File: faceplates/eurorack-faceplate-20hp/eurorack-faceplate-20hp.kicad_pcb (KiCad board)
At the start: 2 copper layers, 101.3 x 133.3 mm, 4 parts

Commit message: Moving mounting holes
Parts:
- moved REF** 2.42 mm to (5.08, 130.3)
- moved REF** 2.42 mm to (5.08, 3.00)
- moved REF** 2.36 mm to (96.2, 130.3)
- moved REF** 2.36 mm to (96.2, 3.00)
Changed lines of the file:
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@@
   (net 0 "")
   (footprint "MountingHole:MountingHole_3.2mm_M3" (layer "F.Cu")
-    (at 7.5 130.35)
+    (at 5.08 130.35)
     (descr "Mounting Hole 3.2mm, no annular, M3")
     (tags "mounting hole 3.2mm no annular m3")
@@
   )
   (footprint "MountingHole:MountingHole_3.2mm_M3" (layer "F.Cu")
-    (at 93.86 130.35)
+    (at 96.22 130.35)
     (descr "Mounting Hole 3.2mm, no annular, M3")
     (tags "mounting hole 3.2mm no annular m3")
@@
   )
   (footprint "MountingHole:MountingHole_3.2mm_M3" (layer "F.Cu")
-    (at 93.86 3)
+    (at 96.22 3)
     (descr "Mounting Hole 3.2mm, no annular, M3")
     (tags "mounting hole 3.2mm no annular m3")
@@
   )
   (footprint "MountingHole:MountingHole_3.2mm_M3" (layer "F.Cu")
-    (at 7.5 3)
+    (at 5.08 3)
     (descr "Mounting Hole 3.2mm, no annular, M3")
     (tags "mounting hole 3.2mm no annular m3")

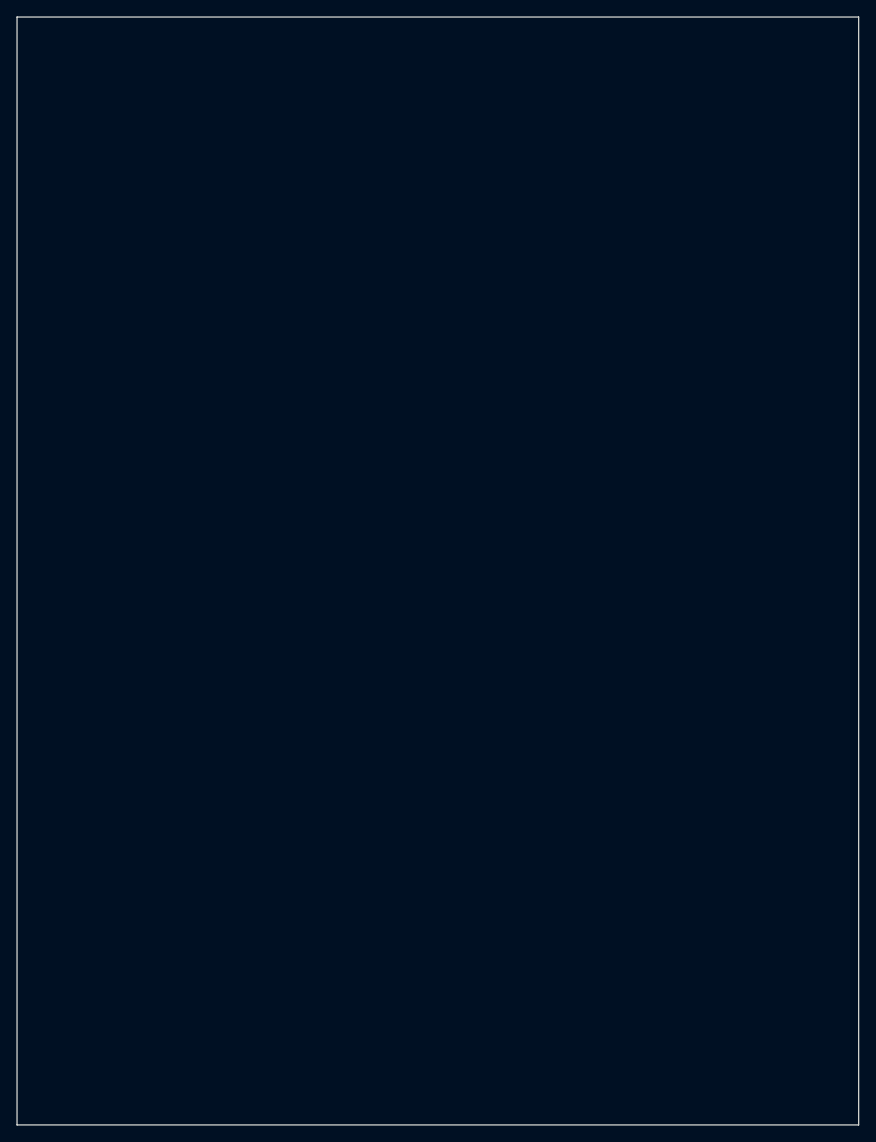
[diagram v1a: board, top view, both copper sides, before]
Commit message: Correcting panel height
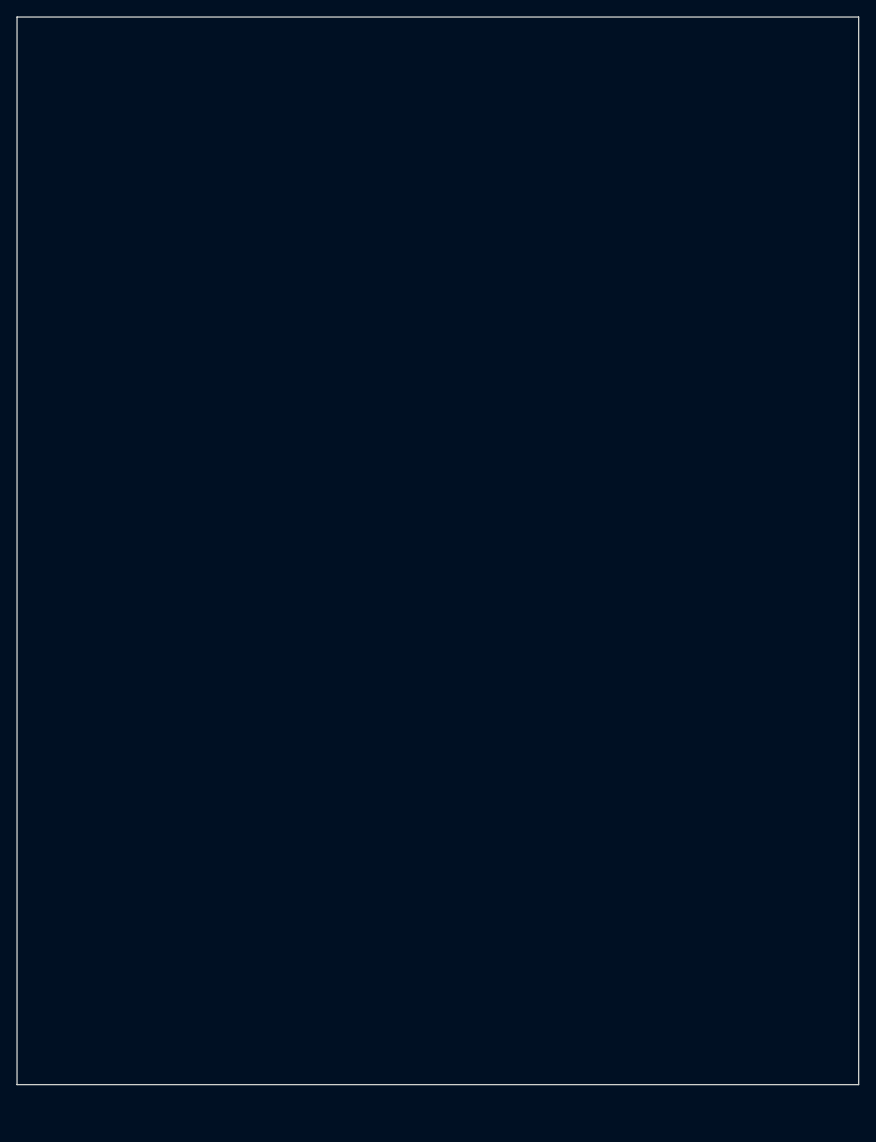
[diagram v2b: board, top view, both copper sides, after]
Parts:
- moved REF** 4.85 mm to (5.08, 125.5)
- moved REF** 4.85 mm to (96.2, 125.5)
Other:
- board size 101.3 x 133.3 mm -> 101.3 x 128.5 mm
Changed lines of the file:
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@@
   (net 0 "")
   (footprint "MountingHole:MountingHole_3.2mm_M3" (layer "F.Cu")
-    (at 5.08 130.35)
+    (at 5.08 125.5)
     (descr "Mounting Hole 3.2mm, no annular, M3")
     (tags "mounting hole 3.2mm no annular m3")
@@
   )
   (footprint "MountingHole:MountingHole_3.2mm_M3" (layer "F.Cu")
-    (at 96.22 130.35)
+    (at 96.22 125.5)
     (descr "Mounting Hole 3.2mm, no annular, M3")
     (tags "mounting hole 3.2mm no annular m3")
@@
     (pad "" np_thru_hole oval locked (at 0 0) (size 7 3.2) (drill oval 7 3.2) (layers F&B.Cu *.Mask))
   )
-  (gr_line (start 101.3 0) (end 101.3 133.35) (layer "Edge.Cuts") (width 0.1))
-  (gr_line (start 0 133.35) (end 0 0) (layer "Edge.Cuts") (width 0.1))
+  (gr_line (start 101.3 0) (end 101.3 128.5) (layer "Edge.Cuts") (width 0.1))
+  (gr_line (start 0 128.5) (end 0 0) (layer "Edge.Cuts") (width 0.1))
   (gr_line (start 0 0) (end 101.3 0) (layer "Edge.Cuts") (width 0.1))
-  (gr_line (start 101.3 133.35) (end 0 133.35) (layer "Edge.Cuts") (width 0.1))
+  (gr_line (start 101.3 128.5) (end 0 128.5) (layer "Edge.Cuts") (width 0.1))
 )
